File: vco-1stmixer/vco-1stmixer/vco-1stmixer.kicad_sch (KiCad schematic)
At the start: 48 parts, among them J101 VCO Control In, J102 1st IF Out, J103 VCO Sample, J104 RF In, J105 Conn_01x02, U101 POS-200, U102 MAV-11, U103 MAV-11, U104 TUF-1H+

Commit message: vco-1stmixer bom
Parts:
- H101, H102, H103, H104: now left out of the parts list
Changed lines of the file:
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@@
   )
   (symbol (lib_id "Mechanical:MountingHole") (at 53.975 22.86 0) (unit 1)
-    (in_bom yes) (on_board yes) (fields_autoplaced)
+    (in_bom no) (on_board yes) (fields_autoplaced)
     (property "Reference" "H103" (id 0) (at 56.515 21.5899 0)
       (effects (font (size 1.27 1.27)) (justify left))
@@
   )
   (symbol (lib_id "Mechanical:MountingHole") (at 73.025 22.86 0) (unit 1)
-    (in_bom yes) (on_board yes) (fields_autoplaced)
+    (in_bom no) (on_board yes) (fields_autoplaced)
     (property "Reference" "H104" (id 0) (at 75.565 21.5899 0)
       (effects (font (size 1.27 1.27)) (justify left))
@@
   )
   (symbol (lib_id "Mechanical:MountingHole") (at 36.195 22.86 0) (unit 1)
-    (in_bom yes) (on_board yes) (fields_autoplaced)
+    (in_bom no) (on_board yes) (fields_autoplaced)
     (property "Reference" "H102" (id 0) (at 38.735 21.5899 0)
       (effects (font (size 1.27 1.27)) (justify left))
@@
   )
   (symbol (lib_id "Mechanical:MountingHole") (at 18.415 22.86 0) (unit 1)
-    (in_bom yes) (on_board yes) (fields_autoplaced)
+    (in_bom no) (on_board yes) (fields_autoplaced)
     (property "Reference" "H101" (id 0) (at 20.955 21.5899 0)
       (effects (font (size 1.27 1.27)) (justify left))

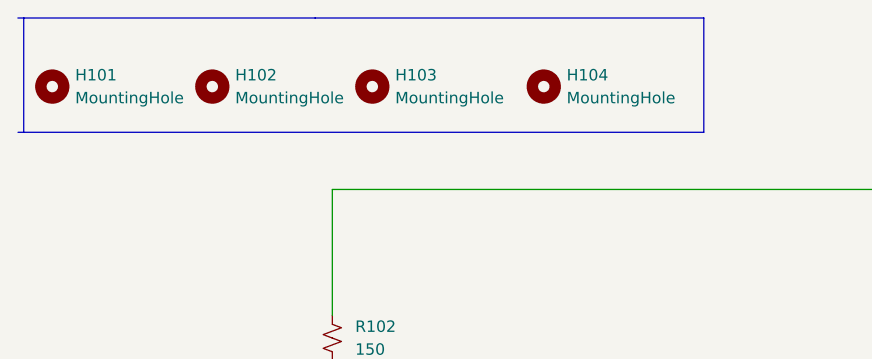
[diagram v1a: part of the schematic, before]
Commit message: Hierarchical schematic updates
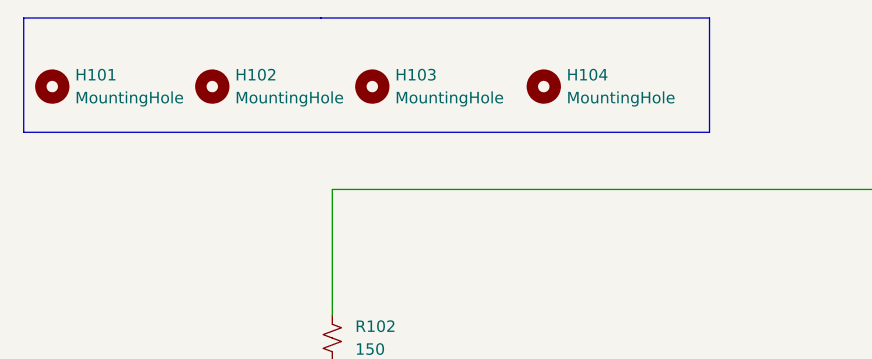
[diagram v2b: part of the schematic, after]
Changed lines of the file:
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@@
     (stroke (width 0) (type default) (color 0 0 0 0))
   )
-  (polyline (pts (xy 90.805 27.94) (xy 14.605 27.94))
+  (polyline (pts (xy 91.44 27.94) (xy 15.24 27.94))
     (stroke (width 0) (type default) (color 0 0 0 0))
   )
@@
     (stroke (width 0) (type default) (color 0 0 0 0))
   )
-  (polyline (pts (xy 47.625 15.24) (xy 90.805 15.24))
+  (polyline (pts (xy 48.26 15.24) (xy 91.44 15.24))
     (stroke (width 0) (type default) (color 0 0 0 0))
   )
@@
     (stroke (width 0) (type default) (color 0 0 0 0))
   )
-  (polyline (pts (xy 47.625 15.24) (xy 14.605 15.24))
+  (polyline (pts (xy 48.26 15.24) (xy 15.24 15.24))
     (stroke (width 0) (type default) (color 0 0 0 0))
   )
@@
     (stroke (width 0) (type default) (color 0 0 0 0))
   )
-  (polyline (pts (xy 90.805 15.24) (xy 90.805 27.94))
-    (stroke (width 0) (type default) (color 0 0 0 0))
-  )
+  (polyline (pts (xy 91.44 15.24) (xy 91.44 27.94))
+    (stroke (width 0) (type default) (color 0 0 0 0))
+  )

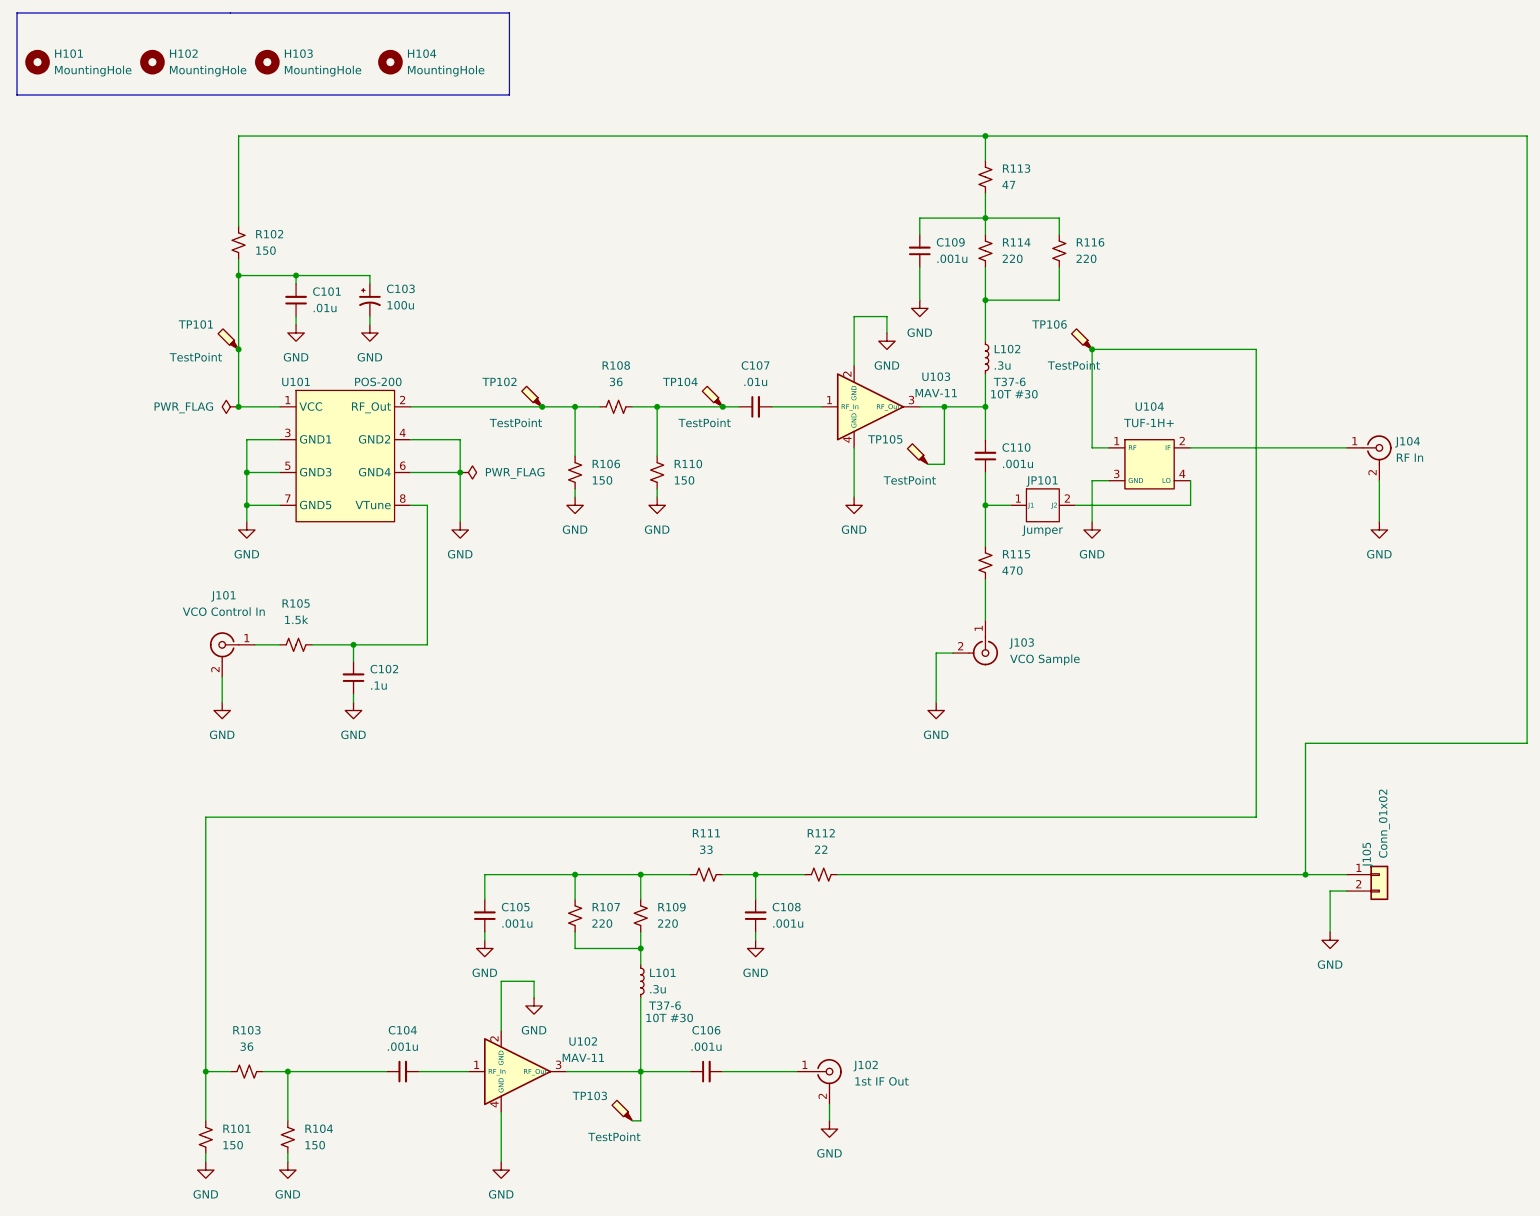
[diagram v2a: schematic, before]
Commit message: minor changes to 5 boards
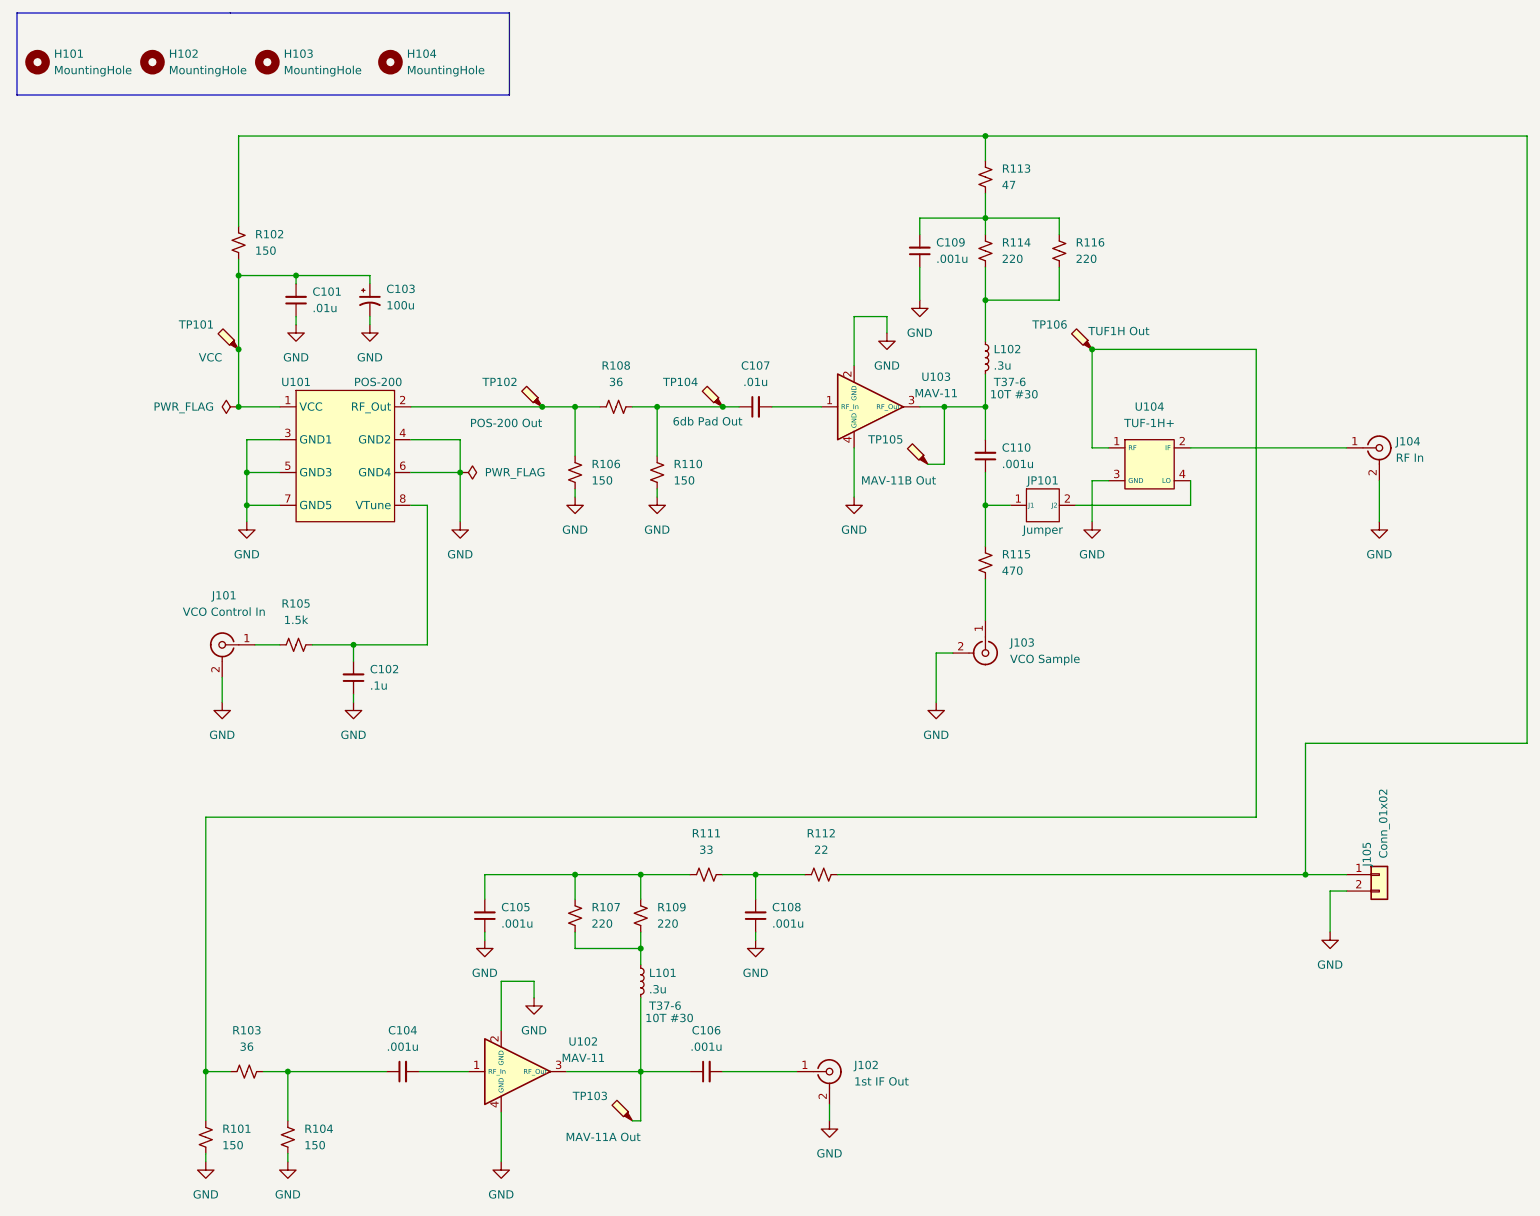
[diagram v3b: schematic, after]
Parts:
- TP101: value TestPoint -> VCC
- TP102: value TestPoint -> POS-200 Out
- TP103: value TestPoint -> MAV-11A Out
- TP104: value TestPoint -> 6db Pad Out
- TP105: value TestPoint -> MAV-11B Out
- TP106: value TestPoint -> TUF1H Out
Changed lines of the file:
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@@
       (effects (font (size 1.27 1.27)) (justify left))
     )
-    (property "Value" "TestPoint" (id 1) (at 46.99 68.58 90)
+    (property "Value" "VCC" (id 1) (at 46.99 68.58 90)
       (effects (font (size 1.27 1.27)) (justify left))
     )
@@
       (effects (font (size 1.27 1.27)) (justify left))
     )
-    (property "Value" "TestPoint" (id 1) (at 96.52 78.74 90)
+    (property "Value" "POS-200 Out" (id 1) (at 96.52 78.74 90)
       (effects (font (size 1.27 1.27)) (justify left))
     )
@@
       (effects (font (size 1.27 1.27)) (justify left))
     )
-    (property "Value" "TestPoint" (id 1) (at 125.73 78.74 90)
+    (property "Value" "6db Pad Out" (id 1) (at 127.508 78.486 90)
       (effects (font (size 1.27 1.27)) (justify left))
     )
@@
       (effects (font (size 1.27 1.27)) (justify left))
     )
-    (property "Value" "TestPoint" (id 1) (at 157.48 87.63 90)
+    (property "Value" "MAV-11B Out" (id 1) (at 157.48 87.63 90)
       (effects (font (size 1.27 1.27)) (justify left))
     )
@@
       (effects (font (size 1.27 1.27)) (justify left))
     )
-    (property "Value" "TestPoint" (id 1) (at 182.88 69.85 90)
+    (property "Value" "TUF1H Out" (id 1) (at 190.5 64.516 90)
       (effects (font (size 1.27 1.27)) (justify left))
     )
@@
       (effects (font (size 1.27 1.27)) (justify left))
     )
-    (property "Value" "TestPoint" (id 1) (at 111.76 189.23 90)
+    (property "Value" "MAV-11A Out" (id 1) (at 111.76 189.23 90)
       (effects (font (size 1.27 1.27)) (justify left))
     )
@@
       (effects (font (size 1.27 1.27)) hide)
     )
-    (property "Datasheet" "" (id 3) (at 66.04 81.28 0)
+    (property "Datasheet" "https://www.mini-circuits.com/pdfs/POS-200+.pdf" (id 3) (at 66.04 81.28 0)
       (effects (font (size 1.27 1.27)) hide)
     )
@@
     )
     (path "/02012ee6-ae0d-45da-8cc9-1a1eea31f966"
-      (reference "TP101") (unit 1) (value "TestPoint") (footprint "TestPoint:TestPoint_Pad_1.0x1.0mm")
+      (reference "TP101") (unit 1) (value "VCC") (footprint "TestPoint:TestPoint_Pad_1.0x1.0mm")
     )
     (path "/05cadbba-8928-447a-9b7a-81720b3f0fa5"
-      (reference "TP102") (unit 1) (value "TestPoint") (footprint "TestPoint:TestPoint_Pad_1.0x1.0mm")
+      (reference "TP102") (unit 1) (value "POS-200 Out") (footprint "TestPoint:TestPoint_Pad_1.0x1.0mm")
     )
     (path "/f0083ef5-b60e-4370-99d5-dc4fb96fd39c"
-      (reference "TP103") (unit 1) (value "TestPoint") (footprint "TestPoint:TestPoint_Pad_1.0x1.0mm")
+      (reference "TP103") (unit 1) (value "MAV-11A Out") (footprint "TestPoint:TestPoint_Pad_1.0x1.0mm")
     )
     (path "/4be822b6-6526-4a22-8c76-b4f384d2954b"
-      (reference "TP104") (unit 1) (value "TestPoint") (footprint "TestPoint:TestPoint_Pad_1.0x1.0mm")
+      (reference "TP104") (unit 1) (value "6db Pad Out") (footprint "TestPoint:TestPoint_Pad_1.0x1.0mm")
     )
     (path "/6eb5c8e7-4692-4739-bec4-37e4fbd2f5fe"
-      (reference "TP105") (unit 1) (value "TestPoint") (footprint "TestPoint:TestPoint_Pad_1.0x1.0mm")
+      (reference "TP105") (unit 1) (value "MAV-11B Out") (footprint "TestPoint:TestPoint_Pad_1.0x1.0mm")
     )
     (path "/be2d0941-b546-4d46-a0c0-0c886ed659e3"
-      (reference "TP106") (unit 1) (value "TestPoint") (footprint "TestPoint:TestPoint_Pad_1.0x1.0mm")
+      (reference "TP106") (unit 1) (value "TUF1H Out") (footprint "TestPoint:TestPoint_Pad_1.0x1.0mm")
     )
     (path "/f7c0561f-3557-4ca5-b7db-ed90d55b045e"

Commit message: v7 conversion
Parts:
- J105: Spice_Model Conn_01x02 -> (none); Spice_Netlist_Enabled N -> (none); Spice_Primitive J -> (none)
- JP101: Spice_Model 22284028 -> (none); Spice_Netlist_Enabled N -> (none); Spice_Primitive J -> (none)
- TP101: value VCC -> ${SIM.PARAMS}; Spice_Netlist_Enabled N -> (none)
- TP102: value POS-200 Out -> ${SIM.PARAMS}; Spice_Netlist_Enabled N -> (none)
- TP103: value MAV-11A Out -> ${SIM.PARAMS}; Spice_Netlist_Enabled N -> (none)
- TP104: value 6db Pad Out -> ${SIM.PARAMS}; Spice_Netlist_Enabled N -> (none)
- TP105: value MAV-11B Out -> ${SIM.PARAMS}; Spice_Netlist_Enabled N -> (none)
- TP106: value TUF1H Out -> ${SIM.PARAMS}; Spice_Netlist_Enabled N -> (none)

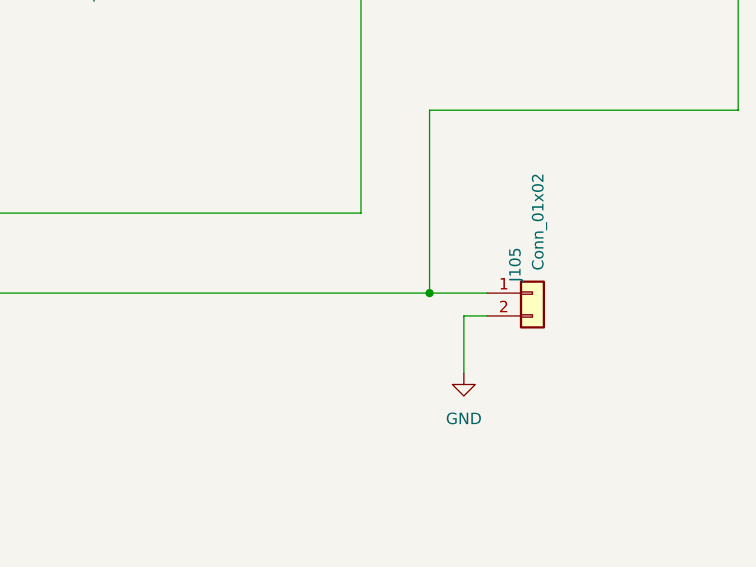
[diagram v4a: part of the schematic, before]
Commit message: updates to hierarchical schematic
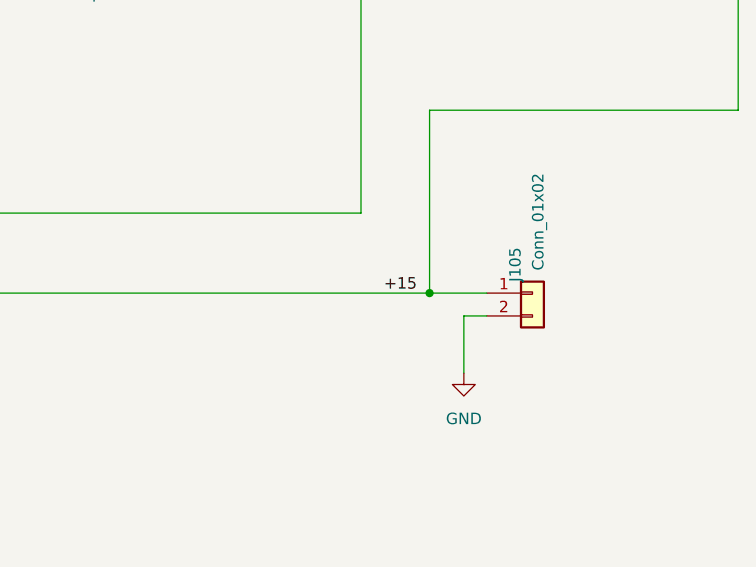
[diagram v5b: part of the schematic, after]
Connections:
- net +15: now reaches J105.1 (Pin_1), R102.2, R112.2, R113.2
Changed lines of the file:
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@@
     (stroke (width 0) (type default))
+  )
+  (label "+15" (at 209.55 148.59 0) (fields_autoplaced)
+    (effects (font (size 1.27 1.27)) (justify left bottom))
   )
   (symbol (lib_id "Connector:TestPoint_Probe") (at 49.53 67.31 90) (unit 1)

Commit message: 1st mixer VCO pcb rev 2
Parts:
- added C111: .001, spectrum-analyzer:DSS1N_MUR, symbol Device:C_Feedthrough
- added TP107: ${SIM.PARAMS}, TestPoint:TestPoint_Pad_1.0x1.0mm, symbol Connector:TestPoint_Probe
- added V101: 15, symbol Simulation_SPICE:VDC
- J103: footprint Connector_Wire:SolderWire-0.5sqmm_1x02_P4.6mm_D0.9mm_OD2.1mm -> Connector_PinHeader_2.54mm:PinHeader_1x02_P2.54mm_Vertical
- J105: footprint vco-1stmixer:691103110002 -> Connector_Wire:SolderWire-0.5sqmm_1x02_P4.6mm_D0.9mm_OD2.1mm
- JP101: Spice_Netlist_Enabled (none) -> N
- TP102: value ${SIM.PARAMS} -> POS-200 Out
- TP103: value ${SIM.PARAMS} -> MAV-11 TUF
- TP105: value ${SIM.PARAMS} -> MAV-11 POS
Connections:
- net +15: now also C111.3, V101.1; no longer R112.2
- net GND: now also C111.2, V101.2
- net at C104.1, R103.2, R104.2: now also TP107.1
- new net: C111.1, R112.2
